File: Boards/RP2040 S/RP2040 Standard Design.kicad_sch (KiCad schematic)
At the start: 40 parts, among them J1 BM03B-SRSS-TBLFSN, J2 DX07S016JA1R1500, U1 W25Q128JVSIQ TR, U11 ST1L05APU33R, U2 ESD7L5.0DT5G

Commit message: Repo Refactor and new systems update
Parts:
- removed D1: PMEG2010ER, PMEG2010ER:SODFL3517X110N, symbol Schottky Diode:PMEG2010ER
- removed J1: BM03B-SRSS-TBLFSN, SWD_Con:CONN_BM03B-SRSS-TBLFSN_JST, symbol SWD Connector:BM03B-SRSS-TBLFSN
- removed J2: DX07S016JA1R1500, USBC-DX07S016JA1:JAE_DX07S016JA1R1500, symbol DX07S016JA1R1500:DX07S016JA1R1500
- removed LED1: HSMH-H191, MAG LIS2MDLTR:LGA-12_2X2X1_STM, symbol Red SMD LED:HSMH-H191
- removed R13: 120, RC0402N_VIS:RC0402N_VIS, symbol Device:R
- removed RC1: 5k1, R_0805_5K1:R_0805_5K1, symbol Device:R
- removed U1: W25Q128JVSIQ TR, NOR Flash:SOIC_208MIL_WIN, symbol 16MB Flash Memory:W25Q128JVSIQ_TR
- removed U11: ST1L05APU33R, LDO ST1L05A:DFN_5APU33R_STM, symbol LDO 5V 3V3:ST1L05APU33R
- removed U2: ESD7L5.0DT5G, ESD7L5-Diode:SOT-723_0P85X1P25_ONS, symbol ESD Diodes:ESD7L5.0DT5G
- removed XTAL1: ASE-12.000MHZ-LC-T, AS12MHz:ASE-3.2X2.5_ABR, symbol Powered Crystal:ASE-12.000MHZ-LC-T
- added CR1: VLMC3100-GS08, LED_PLCC_VSMB, symbol GreenLED__VLMC3100-GS08:VLMC3100-GS08
- added D1: PMEG2010ER, PMEG2010ER:SODFL3517X110N, symbol PMEG2010ER:PMEG2010ER
- added J2: BM03B-SRSS-TBLFSN, CONN_BM03B-SRSS-TBLFSN_JST, symbol SWD_Con:BM03B-SRSS-TBLFSN
- added J4: DX07S016JA1R1500, DX07S016JA1R1500:JAE_DX07S016JA1R1500, symbol DX07S016JA1R1500:DX07S016JA1R1500
- added R10: 1k, RES_0402:RES_0402, symbol Device:R
- added R11: 5k1, R_0805_5K1:R_0805_5K1, symbol Device:R
- added U1: W25Q128JVSIQ TR, SOIC_208MIL_WIN, symbol 16MB_Flash:W25Q128JVSIQ_TR
- added U2: ESD7L5.0DT5G, SOT-723_0P85X1P25_ONS, symbol ESD7L5_Diode:ESD7L5.0DT5G
- added U3: ST1L05APU33R, DFN_5APU33R_STM, symbol LDO_ST1L05A:ST1L05APU33R
- added XTAL1: ASE-12.000MHZ-LC-T, ASE-3.2X2.5_ABR, symbol AS12MHz:ASE-12.000MHZ-LC-T
- R8: value 1k -> 650; footprint RES_0402:RES_0402 -> (none)
- S1, S2: footprint E-Switch_7mm:SW_TL3305CF160QG -> TL3305CF160QG:SW_TL3305CF160QG
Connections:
- net +3.3V: now also U1.8 (VCC), U3.2 (V0), XTAL1.4 (VDD)
- net +5V: now also D1.C, U3.3 (V1)
- net CRYSTAL: now also XTAL1.3 (OUTPUT)
- net GND: now also CR1.1, J2.2, J4.1 (GND), J4.12 (GND), R11.1, U1.4 (GND), U2.3, U3.6 (GND), U3.7 (GND), XTAL1.2 (GND/CASE)
- net MCU QSPI_SCLK: now also U1.6 (CLK)
- net MCU QSPI_SD0: now also U1.5 (DI(IO0))
- net MCU QSPI_SD1: now also U1.2 (DO(IO1))
- net MCU QSPI_SD2: now also U1.3 (/WP(IO2))
- net MCU QSPI_SD3: now also U1.7 (/HOLD_/RESET)
- net MCU QSPI_SS: now also R10.2, U1.1 (/CS); no longer R8.2
- net USB_DM: now also J4.5 (D-), J4.8 (D-), U2.1
- net USB_DP: now also J4.6 (D+), J4.7 (D+), U2.2
- net ~{USB_BOOT}: now also R10.1; no longer R8.1
- net at R9.2: now also J4.9 (CC2)
- net at R5.1: now also J2.3
- net at R7.1: now also XTAL1.1 (TRI-STATE(STBY))
- net at R4.1: now also J2.1
- net at MCU1.37 (GPIO25): now also R8.1
- net GP12/SPI0 RDY renamed GP12/I2C0 SDA
- net GP13/SPI1 ~{CS} renamed GP13/I2C0 SCL
- net GP14/SPI0 RDY renamed GP14/I2C1 SDA
- net GP15/SPI0 RDY renamed GP15/I2C1 SCL
- net GP21/SPI0 ~{CS} renamed GP21/PWM2 B/CLKOUT 0
- net GP26/SPI1 RDY renamed GP26_ADC0
- net GP29/SPI1 ~{CS} renamed GP29_ADC3
- net GP6/SPI1 RDY renamed GP6/UART1 CTS
- net GPIO23 renamed GP23/PWM3 B/CLKOUT 1
- net GPIO24 renamed GP24/PWM4 A
- net GPIO4 renamed GP4/UART1 TX
- net GPIO5 renamed GP5/UART1 RX
- net GPIO7 renamed GP7/UART1 RTS
- new net: J4.3 (CC1), R11.2
- new net: CR1.2, R8.2
- new net: D1.A, J4.11 (VBUS), J4.2 (VBUS)
- new net: J4.S1 (SHIELD), J4.S2 (SHIELD), J4.S3 (SHIELD), J4.S4 (SHIELD), J4.S5 (SHIELD), J4.S6 (SHIELD)

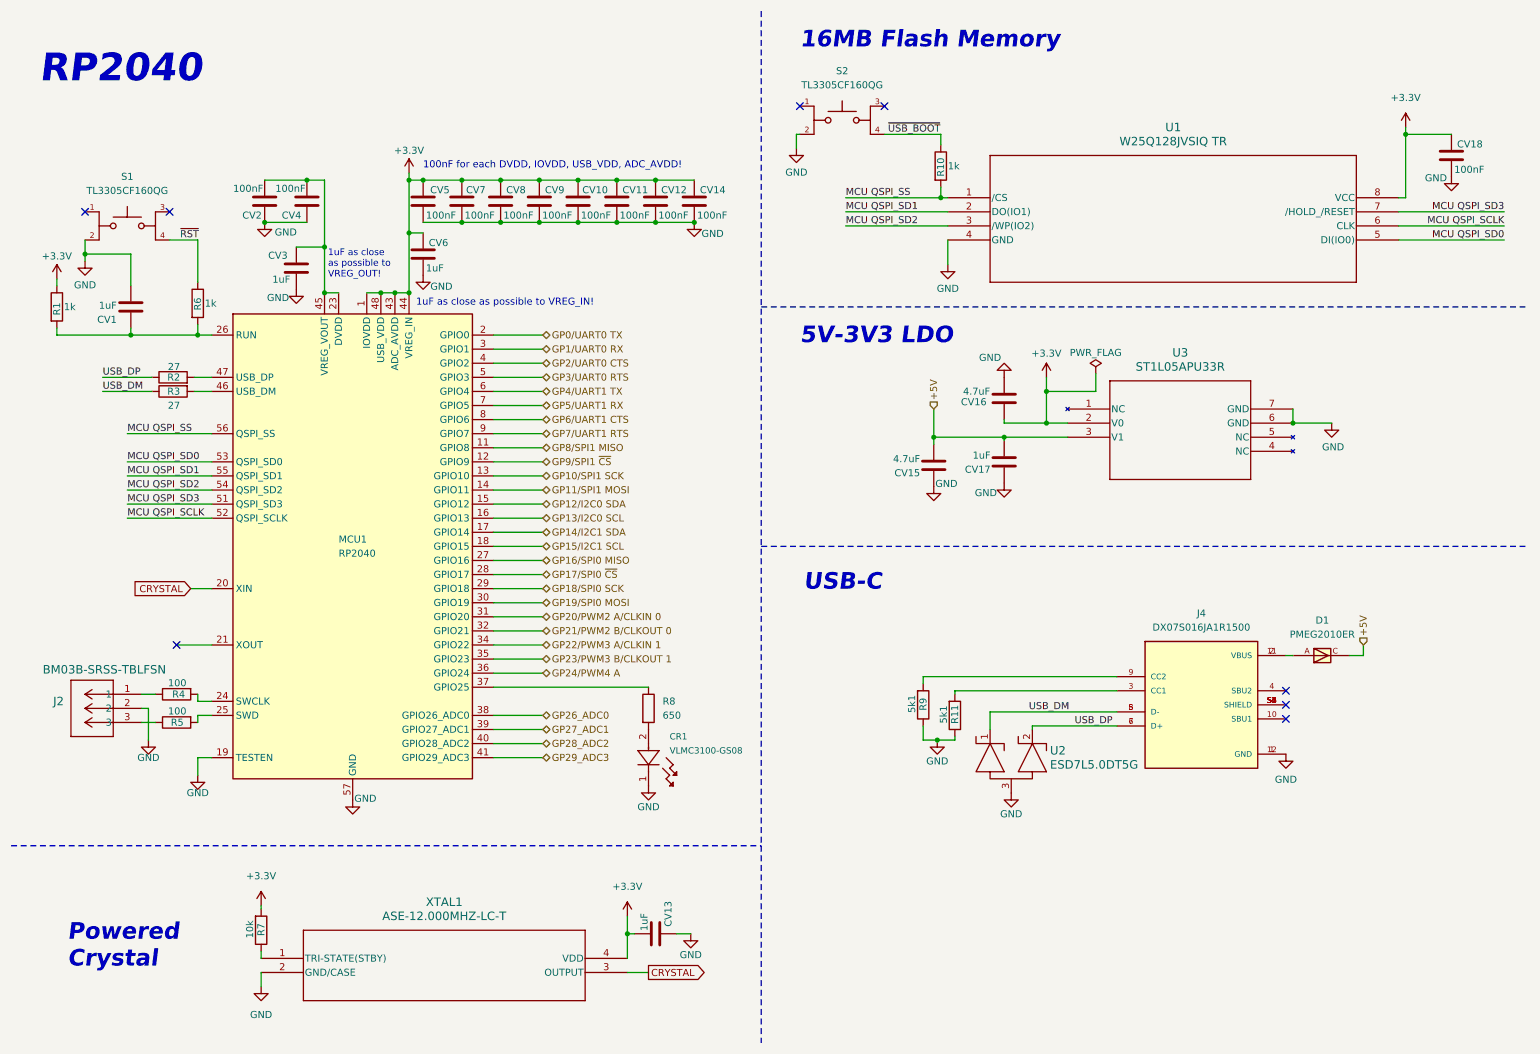
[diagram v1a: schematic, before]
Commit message: Sockets Pico_Conn
Adição à Library e ao RP2040 S de Sockets iguais às placas de Pico.
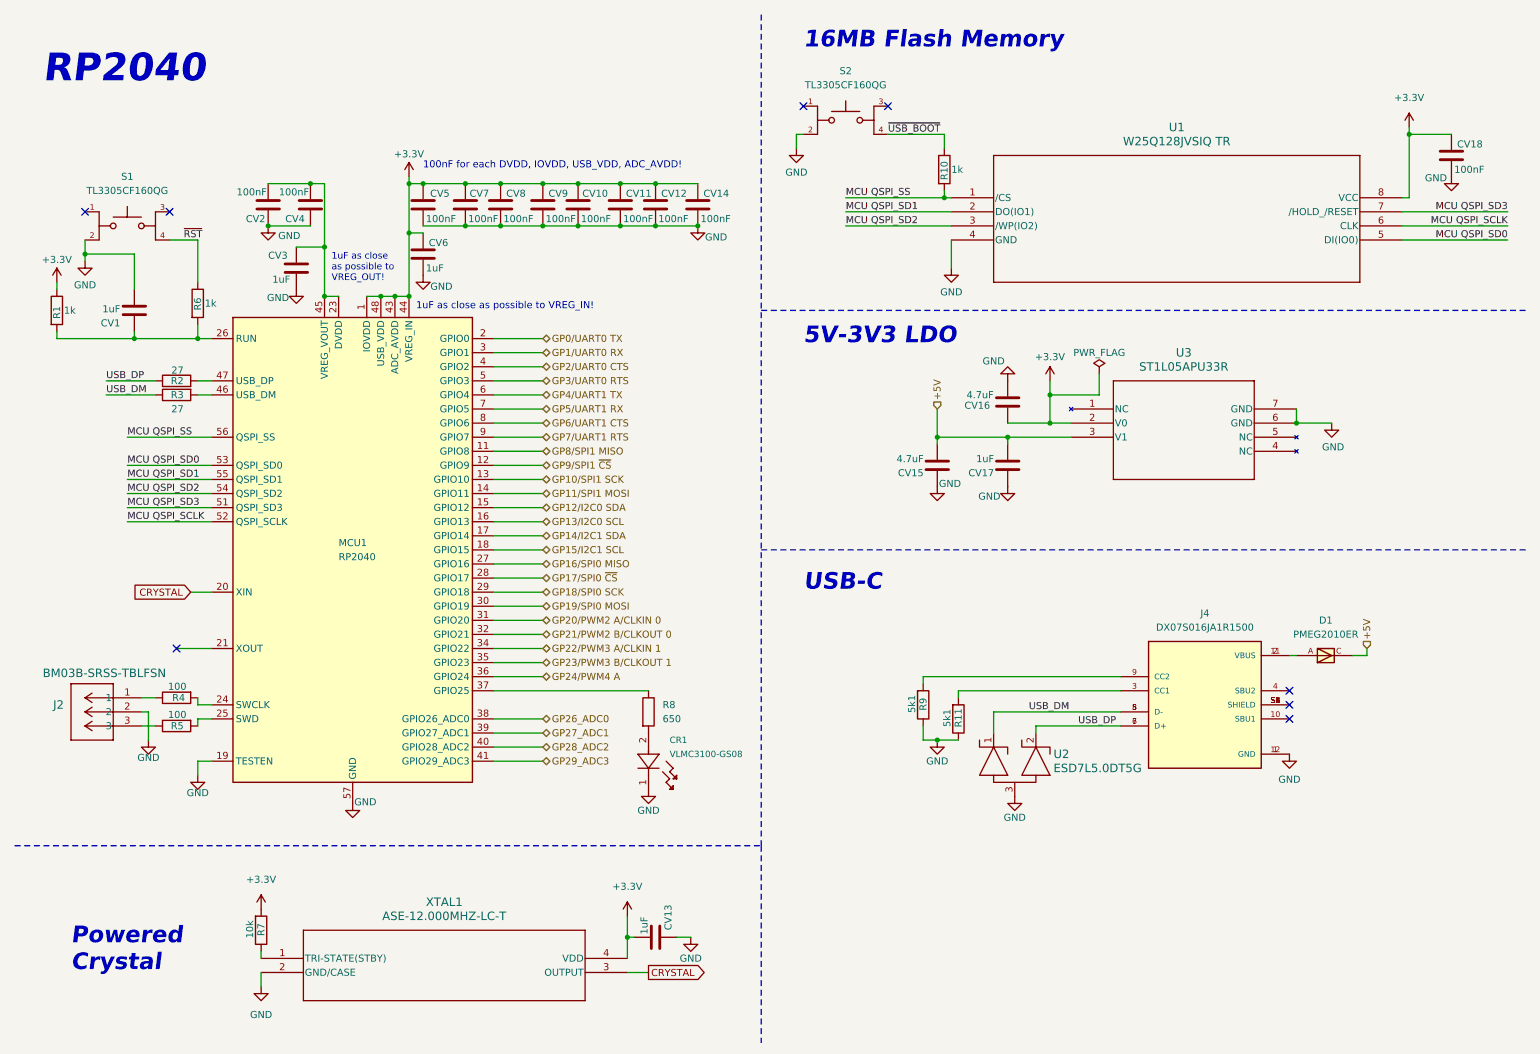
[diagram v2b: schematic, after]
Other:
- moved on the sheet: CR1, CV1, CV10, CV11, CV12, CV13, CV14, CV15, CV16, CV17, CV2, CV4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

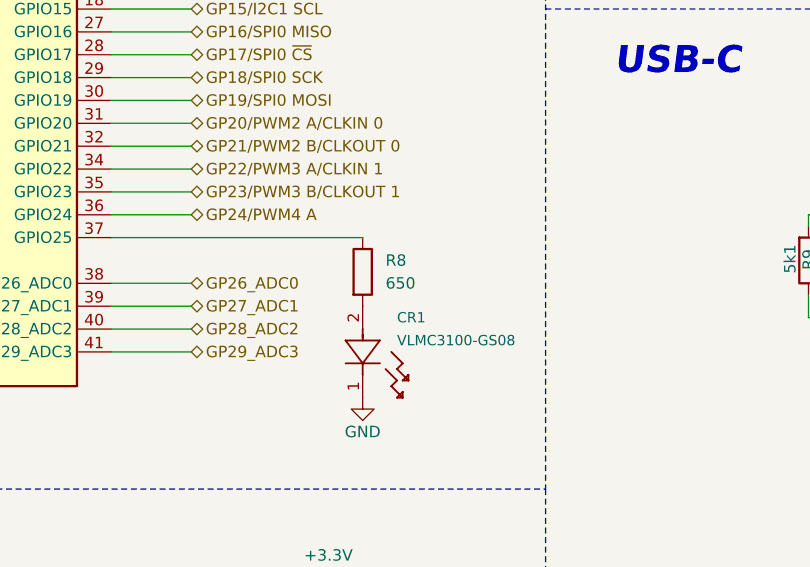
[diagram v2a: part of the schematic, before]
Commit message: RP2040 FOOTPRINTS
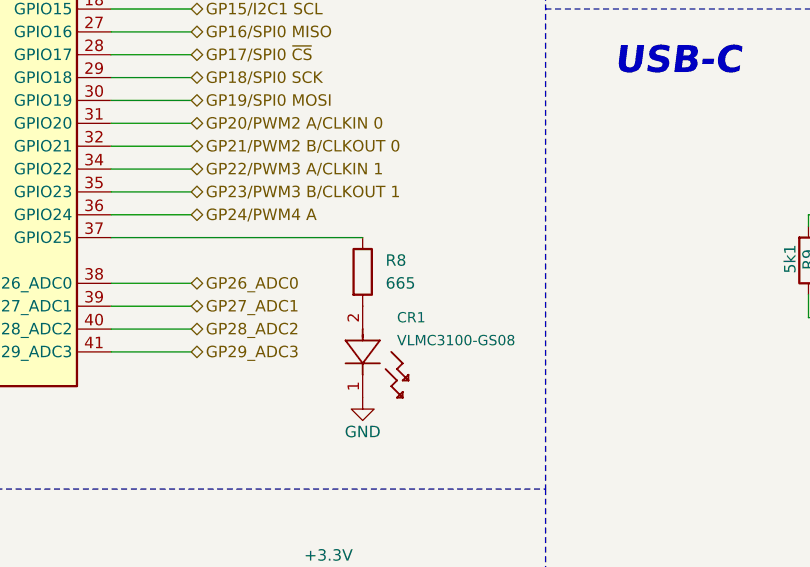
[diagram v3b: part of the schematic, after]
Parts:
- CR1: footprint LED_PLCC_VSMB -> LED-Green_VLMC3100-GS08:LED_PLCC_VSMB
- CV1, CV10, CV11, CV12, CV13, CV14, CV17, CV18, CV2, CV3, CV4, CV5, CV6, CV7, CV8, CV9: footprint Capacitor_0402:Capacitor_0402 -> Capacitor-0402:Capacitor_0402
- CV15, CV16: footprint C_4uF7_0402:C_4uF7_0402 -> Capacitor-0402:Capacitor_0402
- D1: footprint PMEG2010ER:SODFL3517X110N -> Diode-Schottky_PMEG2010ER:SODFL3517X110N
- J2: footprint CONN_BM03B-SRSS-TBLFSN_JST -> SWD_Con:CONN_BM03B-SRSS-TBLFSN_JST
- J4: footprint DX07S016JA1R1500:JAE_DX07S016JA1R1500 -> USBC-DX07S016JA1:JAE_DX07S016JA1R1500
- R1, R10, R4, R5, R6, R7: footprint RES_0402:RES_0402 -> Capacitor-0402:Capacitor_0402
- R11, R9: footprint R_0805_5K1:R_0805_5K1 -> Resistor-0805:R_0805_5K1
- R2, R3: footprint RES_R0603_27:RES_R0603_27 -> Resistor-0603:RES_R0603_27
- R8: value 650 -> 665; footprint (none) -> Capacitor-0402:Capacitor_0402
- S1, S2: footprint TL3305CF160QG:SW_TL3305CF160QG -> E-Switch_7mm:SW_TL3305CF160QG
- U1: footprint SOIC_208MIL_WIN -> NOR Flash:SOIC_208MIL_WIN
- U2: footprint SOT-723_0P85X1P25_ONS -> ESD7L5-Diode:SOT-723_0P85X1P25_ONS
- U3: footprint DFN_5APU33R_STM -> LDO ST1L05A:DFN_5APU33R_STM
- XTAL1: footprint ASE-3.2X2.5_ABR -> AS12MHz:ASE-3.2X2.5_ABR
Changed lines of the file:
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@@
 			)
 		)
-		(property "Footprint" "RES_0402:RES_0402"
+		(property "Footprint" "Capacitor-0402:Capacitor_0402"
 			(at 55.372 177.8 90)
 			(effects
@@
 			)
 		)
-		(property "Footprint" "Capacitor_0402:Capacitor_0402"
+		(property "Footprint" "Capacitor-0402:Capacitor_0402"
 			(at 33.3248 62.23 0)
 			(effects
@@
 			)
 		)
-		(property "Footprint" "RES_R0603_27:RES_R0603_27"
+		(property "Footprint" "Resistor-0603:RES_R0603_27"
 			(at 41.91 79.502 90)
 			(effects
@@
 			)
 		)
-		(property "Footprint" "Capacitor_0402:Capacitor_0402"
+		(property "Footprint" "Capacitor-0402:Capacitor_0402"
 			(at 87.3252 59.69 0)
 			(effects
@@
 			)
 		)
-		(property "Footprint" "SOT-723_0P85X1P25_ONS"
+		(property "Footprint" "ESD7L5-Diode:SOT-723_0P85X1P25_ONS"
 			(at 194.31 138.43 0)
 			(effects
@@
 			)
 		)
-		(property "Footprint" "RES_0402:RES_0402"
+		(property "Footprint" "Capacitor-0402:Capacitor_0402"
 			(at 41.91 139.192 90)
 			(effects
@@
 			)
 		)
-		(property "Footprint" "RES_0402:RES_0402"
+		(property "Footprint" "Capacitor-0402:Capacitor_0402"
 			(at 178.562 40.64 90)
 			(effects
@@
 			)
 		)
-		(property "Footprint" "Capacitor_0402:Capacitor_0402"
+		(property "Footprint" "Capacitor-0402:Capacitor_0402"
 			(at 108.9152 50.8 0)
 			(effects
@@
 			)
 		)
-		(property "Footprint" "Capacitor_0402:Capacitor_0402"
+		(property "Footprint" "Capacitor-0402:Capacitor_0402"
 			(at 94.9452 50.8 0)
 			(effects
@@
 			)
 		)
-		(property "Footprint" "Capacitor_0402:Capacitor_0402"
+		(property "Footprint" "Capacitor-0402:Capacitor_0402"
 			(at 132.08 178.1048 0)
 			(effects
@@
 			)
 		)
-		(property "Footprint" "R_0805_5K1:R_0805_5K1"
+		(property "Footprint" "Resistor-0805:R_0805_5K1"
 			(at 181.102 139.7 90)
 			(effects
@@
 			)
 		)
-		(property "Footprint" "C_4uF7_0402:C_4uF7_0402"
+		(property "Footprint" "Capacitor-0402:Capacitor_0402"
 			(at 178.1048 90.17 0)
 			(effects
@@
 			)
 		)
-		(property "Footprint" "RES_0402:RES_0402"
+		(property "Footprint" "Capacitor-0402:Capacitor_0402"
 			(at 18.542 66.04 90)
 			(effects
@@
 			)
 		)
-		(property "Value" "650"
+		(property "Value" "665"
 			(at 129.54 139.6999 0)
 			(effects
@@
 			)
 		)
-		(property "Footprint" ""
+		(property "Footprint" "Capacitor-0402:Capacitor_0402"
 			(at 125.222 138.43 90)
 			(effects
@@
 			)
 		)
-		(property "Footprint" "Capacitor_0402:Capacitor_0402"
+		(property "Footprint" "Capacitor-0402:Capacitor_0402"
 			(at 101.2952 50.8 0)
 			(effects
@@
 			)
 		)
-		(property "Footprint" "CONN_BM03B-SRSS-TBLFSN_JST"
+		(property "Footprint" "SWD_Con:CONN_BM03B-SRSS-TBLFSN_JST"
 			(at 35.56 135.89 0)
 			(effects
@@
 			)
 		)
-		(property "Footprint" "LED_PLCC_VSMB"
+		(property "Footprint" "LED-Green_VLMC3100-GS08:LED_PLCC_VSMB"
 			(at 127 142.24 0)
 			(effects
@@
 			)
 		)
-		(property "Footprint" "DX07S016JA1R1500:JAE_DX07S016JA1R1500"
+		(property "Footprint" "USBC-DX07S016JA1:JAE_DX07S016JA1R1500"
 			(at 227.33 135.89 0)
 			(effects
@@
 			)
 		)
-		(property "Footprint" "TL3305CF160QG:SW_TL3305CF160QG"
+		(property "Footprint" "E-Switch_7mm:SW_TL3305CF160QG"
 			(at 33.02 50.8 0)
 			(effects
@@
 			)
 		)
-		(property "Footprint" "Capacitor_0402:Capacitor_0402"
+		(property "Footprint" "Capacitor-0402:Capacitor_0402"
 			(at 129.2352 50.8 0)
 			(effects
@@
 			)
 		)
-		(property "Footprint" "RES_0402:RES_0402"
+		(property "Footprint" "Capacitor-0402:Capacitor_0402"
 			(at 43.942 64.77 90)
 			(effects
@@
 			)
 		)
-		(property "Footprint" "SOIC_208MIL_WIN"
+		(property "Footprint" "NOR Flash:SOIC_208MIL_WIN"
 			(at 181.61 45.72 0)
 			(effects
@@
 			)
 		)
-		(property "Footprint" "Capacitor_0402:Capacitor_0402"
+		(property "Footprint" "Capacitor-0402:Capacitor_0402"
 			(at 115.2652 50.8 0)
 			(effects
@@
 			)
 		)
-		(property "Footprint" "RES_R0603_27:RES_R0603_27"
+		(property "Footprint" "Resistor-0603:RES_R0603_27"
 			(at 41.91 80.518 90)
 			(effects
@@
 			)
 		)
-		(property "Footprint" "ASE-3.2X2.5_ABR"
+		(property "Footprint" "AS12MHz:ASE-3.2X2.5_ABR"
 			(at 57.15 182.88 0)
 			(effects
@@
 			)
 		)
-		(property "Footprint" "Capacitor_0402:Capacitor_0402"
+		(property "Footprint" "Capacitor-0402:Capacitor_0402"
 			(at 65.0748 43.18 0)
 			(effects
@@
 			)
 		)
-		(property "Footprint" "TL3305CF160QG:SW_TL3305CF160QG"
+		(property "Footprint" "E-Switch_7mm:SW_TL3305CF160QG"
 			(at 162.56 31.75 0)
 			(effects
@@
 			)
 		)
-		(property "Footprint" "R_0805_5K1:R_0805_5K1"
+		(property "Footprint" "Resistor-0805:R_0805_5K1"
 			(at 174.752 137.16 90)
 			(effects
@@
 			)
 		)
-		(property "Footprint" "Capacitor_0402:Capacitor_0402"
+		(property "Footprint" "Capacitor-0402:Capacitor_0402"
 			(at 122.8852 50.8 0)
 			(effects
@@
 			)
 		)
-		(property "Footprint" "Capacitor_0402:Capacitor_0402"
+		(property "Footprint" "Capacitor-0402:Capacitor_0402"
 			(at 64.4652 62.23 0)
 			(effects
@@
 			)
 		)
-		(property "Footprint" "Capacitor_0402:Capacitor_0402"
+		(property "Footprint" "Capacitor-0402:Capacitor_0402"
 			(at 136.8552 50.8 0)
 			(effects
@@
 			)
 		)
-		(property "Footprint" "C_4uF7_0402:C_4uF7_0402"
+		(property "Footprint" "Capacitor-0402:Capacitor_0402"
 			(at 190.8048 86.36 0)
 			(effects
@@
 			)
 		)
-		(property "Footprint" "RES_0402:RES_0402"
+		(property "Footprint" "Capacitor-0402:Capacitor_0402"
 			(at 41.91 134.112 90)
 			(effects
@@
 			)
 		)
-		(property "Footprint" "DFN_5APU33R_STM"
+		(property "Footprint" "LDO ST1L05A:DFN_5APU33R_STM"
 			(at 203.2 83.82 0)
 			(effects
@@
 			)
 		)
-		(property "Footprint" "Capacitor_0402:Capacitor_0402"
+		(property "Footprint" "Capacitor-0402:Capacitor_0402"
 			(at 87.3252 50.8 0)
 			(effects
@@
 			)
 		)
-		(property "Footprint" "PMEG2010ER:SODFL3517X110N"
+		(property "Footprint" "Diode-Schottky_PMEG2010ER:SODFL3517X110N"
 			(at 248.92 128.27 0)
 			(effects
@@
 			)
 		)
-		(property "Footprint" "Capacitor_0402:Capacitor_0402"
+		(property "Footprint" "Capacitor-0402:Capacitor_0402"
 			(at 57.4548 43.18 0)
 			(effects
@@
 			)
 		)
-		(property "Footprint" "Capacitor_0402:Capacitor_0402"
+		(property "Footprint" "Capacitor-0402:Capacitor_0402"
 			(at 190.8048 90.17 0)
 			(effects
@@
 			)
 		)
-		(property "Footprint" "Capacitor_0402:Capacitor_0402"
+		(property "Footprint" "Capacitor-0402:Capacitor_0402"
 			(at 272.7452 41.91 0)
 			(effects

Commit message: Footprints (RP2040 Corrigido e OBC)
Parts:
- R1, R10, R4, R5, R6, R7, R8: footprint Capacitor-0402:Capacitor_0402 -> Resistor-0402:RES_0402
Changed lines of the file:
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@@
 			)
 		)
-		(property "Footprint" "Capacitor-0402:Capacitor_0402"
+		(property "Footprint" "Resistor-0402:RES_0402"
 			(at 55.372 177.8 90)
 			(effects
@@
 			)
 		)
-		(property "Footprint" "Capacitor-0402:Capacitor_0402"
+		(property "Footprint" "Resistor-0402:RES_0402"
 			(at 41.91 139.192 90)
 			(effects
@@
 			)
 		)
-		(property "Footprint" "Capacitor-0402:Capacitor_0402"
+		(property "Footprint" "Resistor-0402:RES_0402"
 			(at 178.562 40.64 90)
 			(effects
@@
 			)
 		)
-		(property "Footprint" "Capacitor-0402:Capacitor_0402"
+		(property "Footprint" "Resistor-0402:RES_0402"
 			(at 18.542 66.04 90)
 			(effects
@@
 			)
 		)
-		(property "Footprint" "Capacitor-0402:Capacitor_0402"
+		(property "Footprint" "Resistor-0402:RES_0402"
 			(at 125.222 138.43 90)
 			(effects
@@
 			)
 		)
-		(property "Footprint" "Capacitor-0402:Capacitor_0402"
+		(property "Footprint" "Resistor-0402:RES_0402"
 			(at 43.942 64.77 90)
 			(effects
@@
 			)
 		)
-		(property "Footprint" "Capacitor-0402:Capacitor_0402"
+		(property "Footprint" "Resistor-0402:RES_0402"
 			(at 41.91 134.112 90)
 			(effects

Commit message: Mudanças nas Schematics
- Capacitor-0805 adicionado à library
- Nomes de Passive Components atualizados na library
- Atualizado as footprint dos RP2040 S, OBC, R COMMS
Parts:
- R11, R9: footprint Resistor-0805:R_0805_5K1 -> Resistor-0805:RES_0805
- R2, R3: footprint Resistor-0603:RES_R0603_27 -> Resistor-0603:RES_0603
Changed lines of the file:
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@@
 			)
 		)
-		(property "Footprint" "Resistor-0603:RES_R0603_27"
+		(property "Footprint" "Resistor-0603:RES_0603"
 			(at 41.91 79.502 90)
 			(effects
@@
 			)
 		)
-		(property "Footprint" "Resistor-0805:R_0805_5K1"
+		(property "Footprint" "Resistor-0805:RES_0805"
 			(at 181.102 139.7 90)
 			(effects
@@
 			)
 		)
-		(property "Footprint" "Resistor-0603:RES_R0603_27"
+		(property "Footprint" "Resistor-0603:RES_0603"
 			(at 41.91 80.518 90)
 			(effects
@@
 			)
 		)
-		(property "Footprint" "Resistor-0805:R_0805_5K1"
+		(property "Footprint" "Resistor-0805:RES_0805"
 			(at 174.752 137.16 90)
 			(effects

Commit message: System update
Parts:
- removed S1, S2: TL3305CF160QG, E-Switch_7mm:SW_TL3305CF160QG, symbol TL3305CF160QG:TL3305CF160QG
- added S1, S2: TL1017AABF160QG, TL1017AABF160QG, symbol TL1017AABF160QG:TL1017AABF160QG
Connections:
- net GND: now also S1.1 (COM), S1.G1, S2.1 (COM), S2.G1
- net ~{RST}: now also S1.2 (NO)
- net ~{USB_BOOT}: now also S2.2 (NO)
- no-connect marks 8 -> 4
